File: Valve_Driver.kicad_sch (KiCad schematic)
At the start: 0 parts

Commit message: Move to KiCad v6, redesign circuit for chamber
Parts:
- added C?: 10u, Capacitor_SMD:C_0805_2012Metric, symbol Device:C
- added C?: 100n, Capacitor_SMD:C_0603_1608Metric, symbol Device:C
- added J? (x2): Conn_01x02, Connector_JST:JST_XH_B2B-XH-AM_1x02_P2.50mm_Vertical, symbol Connector_Generic:Conn_01x02
- added U?: TC1508S, Package_SO:SOP-16_3.9x9.9mm_P1.27mm, symbol co2_sensor_node:TC1508S
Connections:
- new net: J?.1 (Pin_1), U?.12 (OUTC)
- new net: J?.2 (Pin_2), U?.13 (OUTB)
- new net: J?.1 (Pin_1), U?.16 (OUTA)
- new net: J?.2 (Pin_2), U?.9 (OUTD)
- new net 3V3_IN: C?.1, C?.1, U?.4 (VDD), U?.8 (VDD)
- new net FWD: U?.2 (INA)
- new net GND: C?.2, C?.2, U?.10 (AGND), U?.11 (PGND), U?.14 (AGND), U?.15 (PGND)
- new net REV: U?.3 (INB)

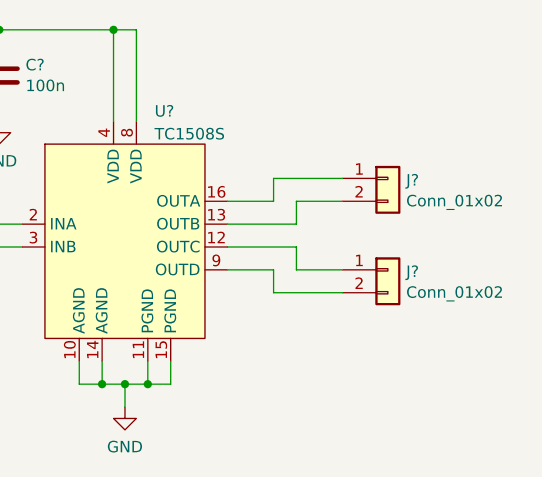
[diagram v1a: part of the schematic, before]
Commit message: Add test points, add JLC part numbers to JST XH connectors, clean up
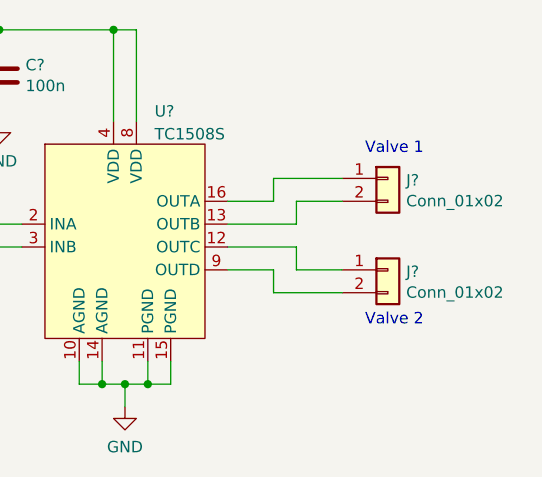
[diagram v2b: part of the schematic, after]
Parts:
- J? (x2): footprint Connector_JST:JST_XH_B2B-XH-AM_1x02_P2.50mm_Vertical -> co2_sensor_node:KF301-5.0-2P
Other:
- note added: "Valve 1"
- note added: "Valve 2"
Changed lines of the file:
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@@
     (stroke (width 0) (type default) (color 0 0 0 0))
+  )
+  (text "Valve 1" (at 166.37 88.9 0)
+    (effects (font (size 1.27 1.27)) (justify left bottom))
+  )
+  (text "Valve 2\n" (at 166.37 107.95 0)
+    (effects (font (size 1.27 1.27)) (justify left bottom))
   )
   (hierarchical_label "FWD" (shape input) (at 123.19 96.52 180)
@@
       (effects (font (size 1.27 1.27)) (justify left))
     )
-    (property "Footprint" "Connector_JST:JST_XH_B2B-XH-AM_1x02_P2.50mm_Vertical" (id 2) (at 168.91 91.44 0)
+    (property "Footprint" "co2_sensor_node:KF301-5.0-2P" (id 2) (at 168.91 91.44 0)
       (effects (font (size 1.27 1.27)) hide)
     )
@@
       (effects (font (size 1.27 1.27)) (justify left))
     )
-    (property "Footprint" "Connector_JST:JST_XH_B2B-XH-AM_1x02_P2.50mm_Vertical" (id 2) (at 168.91 101.6 0)
+    (property "Footprint" "co2_sensor_node:KF301-5.0-2P" (id 2) (at 168.91 101.6 0)
       (effects (font (size 1.27 1.27)) hide)
     )

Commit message: Add testpoint footprint assignments
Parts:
- gave numbers to parts that had none: 5
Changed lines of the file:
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@@
   (symbol (lib_id "Device:C") (at 114.3 80.01 0) (unit 1)
     (in_bom yes) (on_board yes)
-    (property "Reference" "C?" (id 0) (at 117.221 78.8416 0)
+    (property "Reference" "C3" (id 0) (at 117.221 78.8416 0)
       (effects (font (size 1.27 1.27)) (justify left))
     )
@@
   (symbol (lib_id "co2_sensor_node:TC1508S") (at 139.7 87.63 0) (unit 1)
     (in_bom yes) (on_board yes) (fields_autoplaced)
-    (property "Reference" "U?" (id 0) (at 142.9894 83.981 0)
+    (property "Reference" "U1" (id 0) (at 142.9894 83.981 0)
       (effects (font (size 1.27 1.27)) (justify left))
     )
@@
   (symbol (lib_id "power:GND") (at 125.73 85.09 0) (unit 1)
     (in_bom yes) (on_board yes) (fields_autoplaced)
-    (property "Reference" "#PWR?" (id 0) (at 125.73 91.44 0)
+    (property "Reference" "#PWR0125" (id 0) (at 125.73 91.44 0)
       (effects (font (size 1.27 1.27)) hide)
     )
@@
   (symbol (lib_id "power:GND") (at 139.7 116.84 0) (unit 1)
     (in_bom yes) (on_board yes) (fields_autoplaced)
-    (property "Reference" "#PWR?" (id 0) (at 139.7 123.19 0)
+    (property "Reference" "#PWR0123" (id 0) (at 139.7 123.19 0)
       (effects (font (size 1.27 1.27)) hide)
     )
@@
   (symbol (lib_id "Connector_Generic:Conn_01x02") (at 168.91 91.44 0) (unit 1)
     (in_bom yes) (on_board yes)
-    (property "Reference" "J?" (id 0) (at 170.942 91.6432 0)
+    (property "Reference" "J10" (id 0) (at 170.942 91.6432 0)
       (effects (font (size 1.27 1.27)) (justify left))
     )
@@
   (symbol (lib_id "Connector_Generic:Conn_01x02") (at 168.91 101.6 0) (unit 1)
     (in_bom yes) (on_board yes)
-    (property "Reference" "J?" (id 0) (at 170.942 101.8032 0)
+    (property "Reference" "J11" (id 0) (at 170.942 101.8032 0)
       (effects (font (size 1.27 1.27)) (justify left))
     )
@@
   (symbol (lib_id "power:GND") (at 114.3 85.09 0) (unit 1)
     (in_bom yes) (on_board yes) (fields_autoplaced)
-    (property "Reference" "#PWR?" (id 0) (at 114.3 91.44 0)
+    (property "Reference" "#PWR0124" (id 0) (at 114.3 91.44 0)
       (effects (font (size 1.27 1.27)) hide)
     )
@@
   (symbol (lib_id "Device:C") (at 125.73 80.01 0) (unit 1)
     (in_bom yes) (on_board yes)
-    (property "Reference" "C?" (id 0) (at 128.651 78.8416 0)
+    (property "Reference" "C4" (id 0) (at 128.651 78.8416 0)
       (effects (font (size 1.27 1.27)) (justify left))
     )

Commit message: Finalize schematic
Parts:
- removed J10, J11: Conn_01x02, co2_sensor_node:KF301-5.0-2P, symbol Connector_Generic:Conn_01x02
- added C10: 220u, Capacitor_THT:CP_Radial_D8.0mm_P3.50mm, symbol Device:C_Polarized
- added TP16: VALVE_1_REV, TestPoint:TestPoint_Loop_D2.50mm_Drill1.0mm_LowProfile, symbol Connector:TestPoint
- added TP17: VALVE_2_FWD, TestPoint:TestPoint_Loop_D2.50mm_Drill1.0mm_LowProfile, symbol Connector:TestPoint
- added TP18: VALVE_1_FWD, TestPoint:TestPoint_Loop_D2.50mm_Drill1.0mm_LowProfile, symbol Connector:TestPoint
- added TP19: VALVE_2_REV, TestPoint:TestPoint_Loop_D2.50mm_Drill1.0mm_LowProfile, symbol Connector:TestPoint
- renumbered C3 to C11, C4 to C12, U1 to U3
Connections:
- net 3V3_IN: now also C10.1
- net GND: now also C10.2
- net OUT_C: now reaches U3.12 (OUTC)
- net OUT_B: now reaches U3.13 (OUTB)
- net OUT_A: now reaches U3.16 (OUTA)
- net OUT_D: now reaches U3.9 (OUTD)
- net FWD renamed FWD_1
- net FWD_1: now also TP18.1
- net REV renamed REV_1
- net REV_1: now also TP16.1
- new net FWD_2: TP17.1, U3.6 (INC)
- new net REV_2: TP19.1, U3.7 (IND)
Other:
- note added: "1.8 A per ch max"
- note added: "Stagger valve openings to avoid large current spikes"
- note removed: "Valve 1"
- note removed: "Valve 2"
- title: (none) -> CO2 Chamber - Valve Driver
- moved on the sheet: C11, C12

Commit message: Checkpoint
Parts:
- removed C10: 220u, Capacitor_THT:CP_Radial_D8.0mm_P3.50mm, symbol Device:C_Polarized
- added C? (x4): 10n, symbol Device:C
- added R? (x4): 1k, symbol Device:R
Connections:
- net GND: now also C?.2, C?.2, C?.2, C?.2
- net OUT_A: now also R?.1
- net OUT_B: now also R?.1
- net OUT_C: now also R?.1
- net OUT_D: now also R?.1
- new net: C?.1, R?.2 (x4)

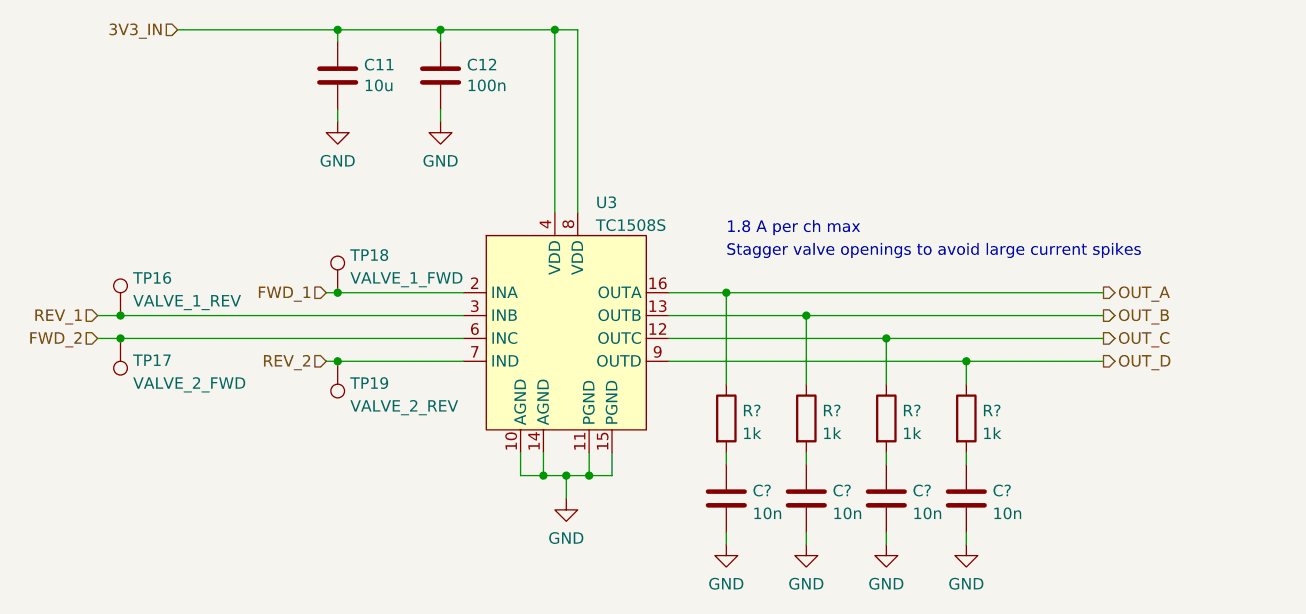
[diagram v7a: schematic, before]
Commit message: Finish rev. 2 schematic and begin PCB layout
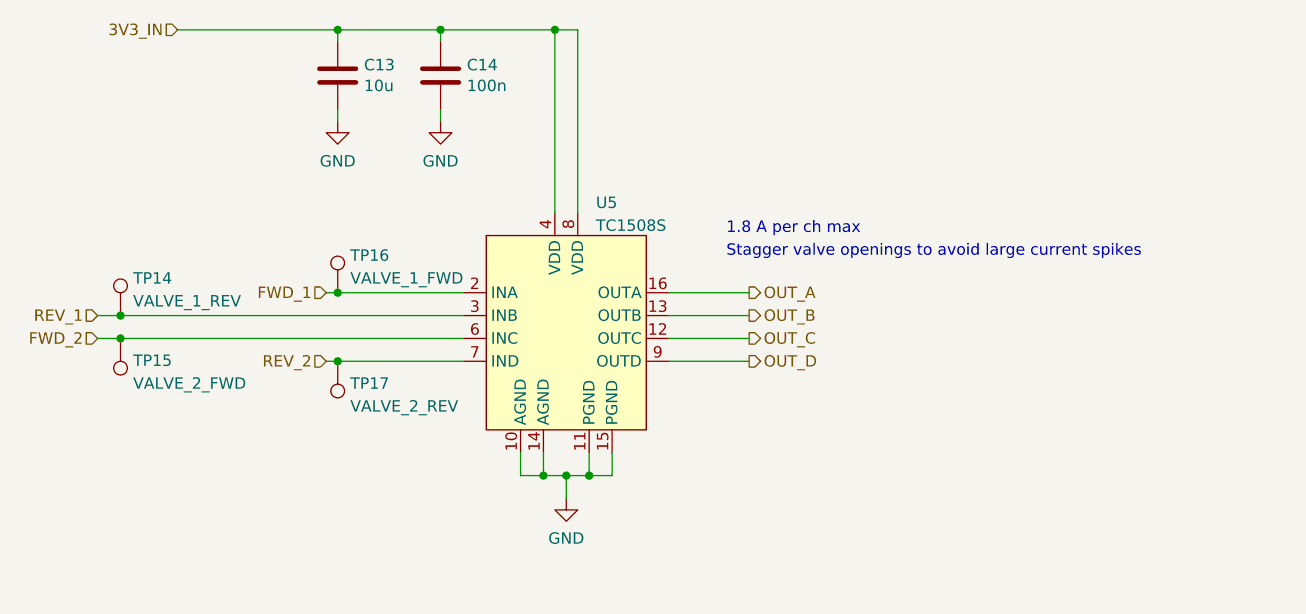
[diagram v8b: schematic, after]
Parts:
- removed C? (x4): 10n, symbol Device:C
- removed R? (x4): 1k, symbol Device:R
- renumbered C11 to C13, C12 to C14, TP16 to TP14, TP17 to TP15, TP18 to TP16, TP19 to TP17, U3 to U5
